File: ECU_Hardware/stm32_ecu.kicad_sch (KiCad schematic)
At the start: 0 parts

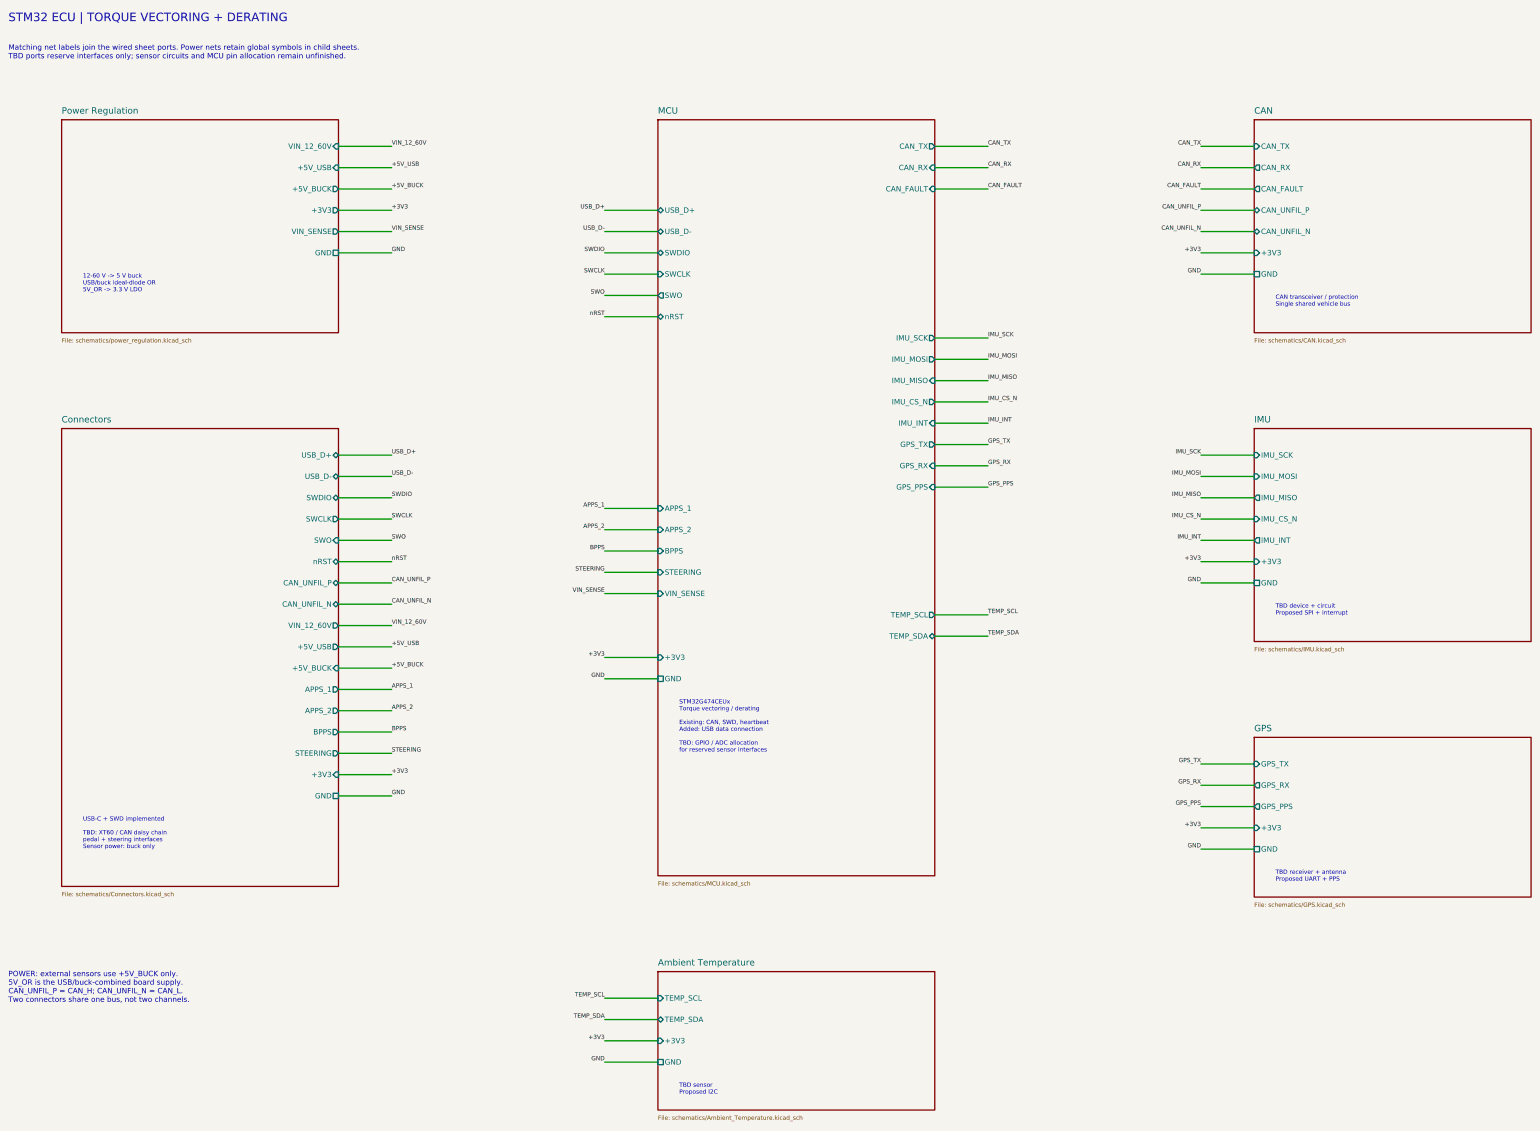
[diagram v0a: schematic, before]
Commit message: Move ECU schematics into schematics/ and add driver inputs and sensor notes
Hierarchical sheets now live in ECU_Hardware/schematics, with the new
Driver_Inputs sheet (APPS, BPPS and steering dividers and clamps), the
reviewed and JLCPCB project symbol libraries, new 3D models, and
SENSOR_INTERFACES.md with the GPS, IMU and temperature pin allocation.
The old top-level sheets and the restore backup are removed.

Claude-Session: https://claude.ai/code/session_0117trEbCv7z6CPYkN3K3GKQ
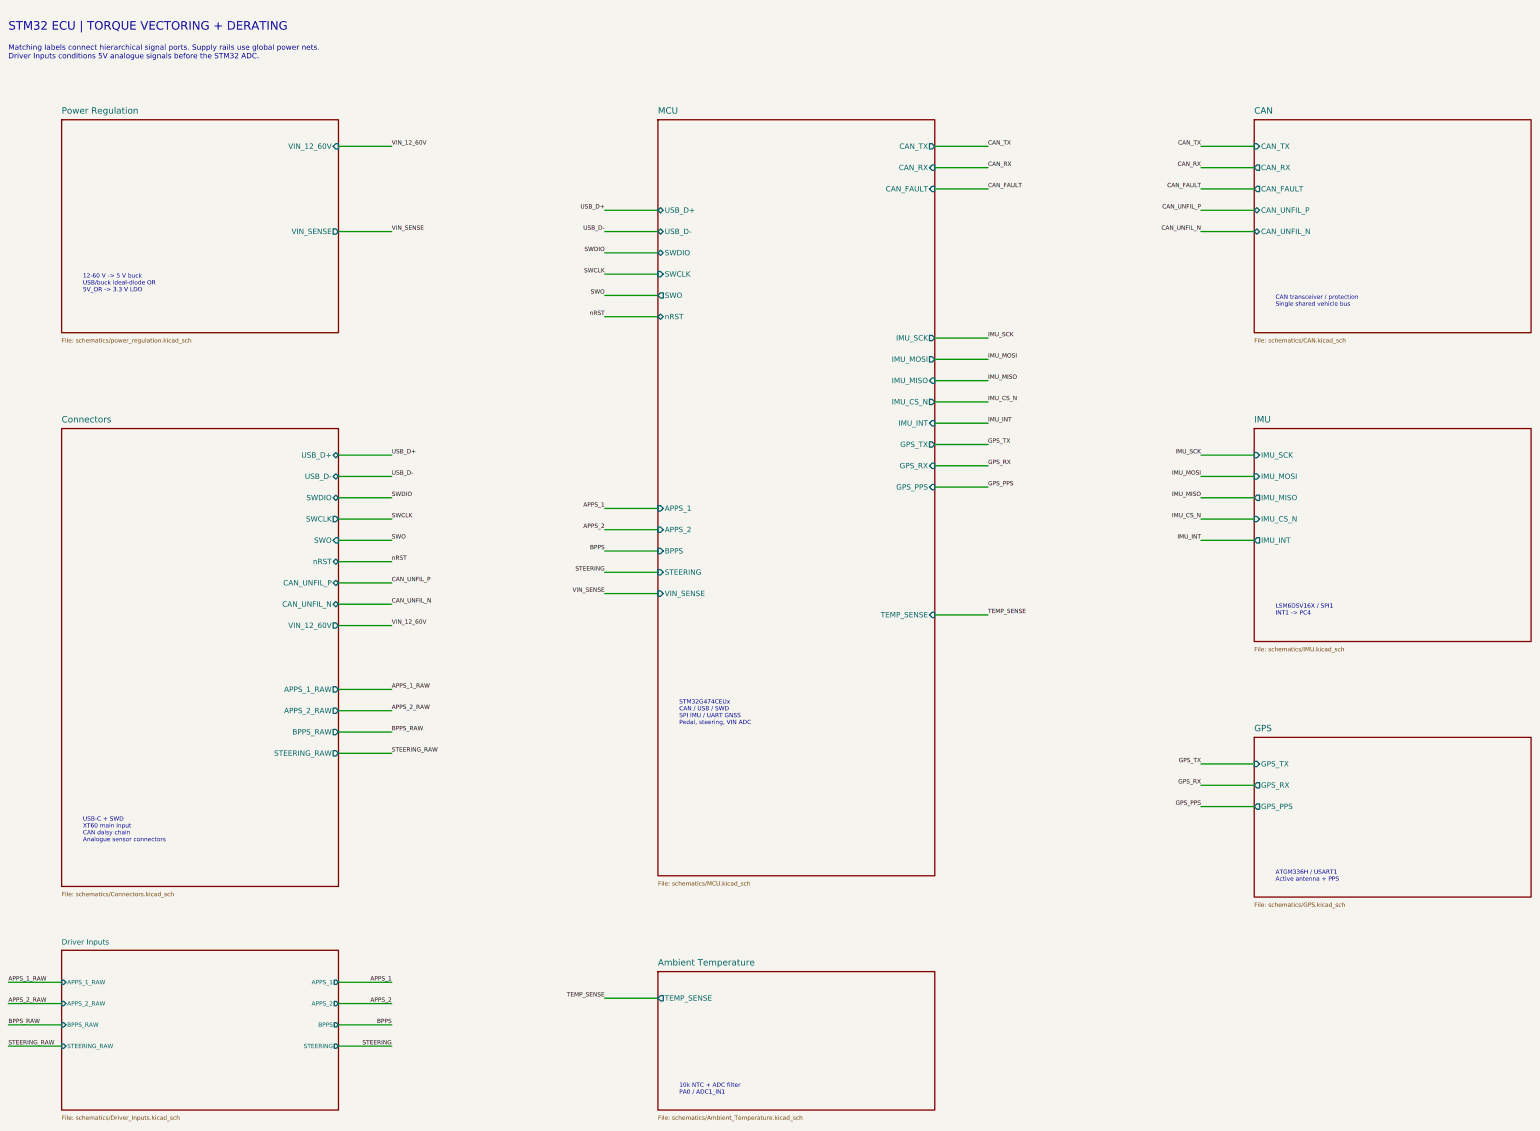
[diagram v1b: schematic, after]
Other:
- added sheet Driver Inputs (schematics/Driver_Inputs.kicad_sch)
- sheet Ambient Temperature ports: added TEMP_SENSE; removed +3V3, GND, TEMP_SCL, TEMP_SDA
- sheet CAN ports: added none; removed +3V3, GND
- sheet Connectors ports: added APPS_1_RAW, APPS_2_RAW, BPPS_RAW, STEERING_RAW; removed +3V3, +5V_BUCK, +5V_USB, APPS_1, APPS_2, BPPS, GND, STEERING
- sheet GPS ports: added none; removed +3V3, GND
- sheet IMU ports: added none; removed +3V3, GND
- sheet MCU ports: added TEMP_SENSE; removed +3V3, GND, TEMP_SCL, TEMP_SDA
- sheet Power Regulation ports: added none; removed +3V3, +5V_BUCK, +5V_USB, GND
- note added: "10k NTC + ADC filter PA0 / ADC1_IN1"
- note added: "ATGM336H / USART1 Active antenna + PPS"
- note added: "LSM6DSV16X / SPI1 INT1 -> PC4"
- note added: "Matching labels connect hierarchical signal ports. Supply rails use global power nets. Driver Inputs conditions 5V analogue signals before the STM32 ADC."
- note added: "STM32G474CEUx CAN / USB / SWD SPI IMU / UART GNSS Pedal, steering, VIN ADC"
- note added: "USB-C + SWD XT60 main input CAN daisy chain Analogue sensor connectors"
- note removed: "Matching net labels join the wired sheet ports. Power nets retain global symbols in child sheets. TBD ports reserve interfaces only; sensor circuits and MCU pin allocation remain unfinished."
- note removed: "POWER: external sensors use +5V_BUCK only. 5V_OR is the USB/buck-combined board supply. CAN_UNFIL_P = CAN_H; CAN_UNFIL_N = CAN_L. Two connectors share one bus, not two channels."
- note removed: "STM32G474CEUx Torque vectoring / derating Existing: CAN, SWD, heartbeat Added: USB data connection TBD: GPIO / ADC allocation for reserved sensor interfaces"
- note removed: "TBD device + circuit Proposed SPI + interrupt"
- note removed: "TBD receiver + antenna Proposed UART + PPS"
- note removed: "TBD sensor Proposed I2C"
- note removed: "USB-C + SWD implemented TBD: XT60 / CAN daisy chain pedal + steering interfaces Sensor power: buck only"
